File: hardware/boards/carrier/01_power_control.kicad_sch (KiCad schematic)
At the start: 34 parts, among them Q1 IPB020N10N5LF, Q2 2N7002, Q3 2N7002, U3 LMX5069MS, U4 INA237AIDGSR, U5 TCAN3413DR

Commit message: Update carrier for 1 oz fabrication
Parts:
- U3: footprint mini-rack-power:MSOP-10_3x3mm_P0.5mm_0.20mm_Clearance -> Package_SO:MSOP-10_3x3mm_P0.5mm
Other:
- note added: "U3 STOCK MSOP-10 FOOTPRINT U3 is Maxinmicro LMX5069MS (C47967145), MSOP-10; manufacturer datasheet is archived locally. Use Package_SO:MSOP-10_3x3mm_P0.5mm. Its 0.15 mm pad-to-pad gap is covered by a footprint-local board clearance override and is compatible with the selected 1 oz outer-copper fabrication process. Confirm vendor DFM before release."
- note removed: "PROJECT-LOCAL U3 FOOTPRINT U3 is Maxinmicro LMX5069MS (C47967145), MSOP-10; manufacturer datasheet is archived locally. Use mini-rack-power:MSOP-10_3x3mm_P0.5mm_0.20mm_Clearance. It retains KiCad's pad length, body, and courtyard, but narrows pads to 0.30 mm for 0.20 mm copper clearance at 0.50 mm pitch. This avoids the stock footprint's 0.15 mm clearance limit with 2 oz copper and satisfies the 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"
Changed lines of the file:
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@@
 		)
 	)
-	(text "PROJECT-LOCAL U3 FOOTPRINT\nU3 is Maxinmicro LMX5069MS (C47967145), MSOP-10; manufacturer datasheet is archived locally.\nUse mini-rack-power:MSOP-10_3x3mm_P0.5mm_0.20mm_Clearance. It retains KiCad's pad length, body, and courtyard,\nbut narrows pads to 0.30 mm for 0.20 mm copper clearance at 0.50 mm pitch. This avoids the stock footprint's 0.15 mm\nclearance limit with 2 oz copper and satisfies the project DRC rule. Confirm final copper weight and vendor DFM before release."
+	(text "U3 STOCK MSOP-10 FOOTPRINT\nU3 is Maxinmicro LMX5069MS (C47967145), MSOP-10; manufacturer datasheet is archived locally.\nUse Package_SO:MSOP-10_3x3mm_P0.5mm. Its 0.15 mm pad-to-pad gap is covered by a footprint-local board clearance\noverride and is compatible with the selected 1 oz outer-copper fabrication process. Confirm vendor DFM before release."
 		(exclude_from_sim no)
 		(at 93.98 76.2 0)
@@
 			)
 		)
-		(property "Footprint" "mini-rack-power:MSOP-10_3x3mm_P0.5mm_0.20mm_Clearance"
+		(property "Footprint" "Package_SO:MSOP-10_3x3mm_P0.5mm"
 			(at 148.59 28.956 0)
 			(hide yes)

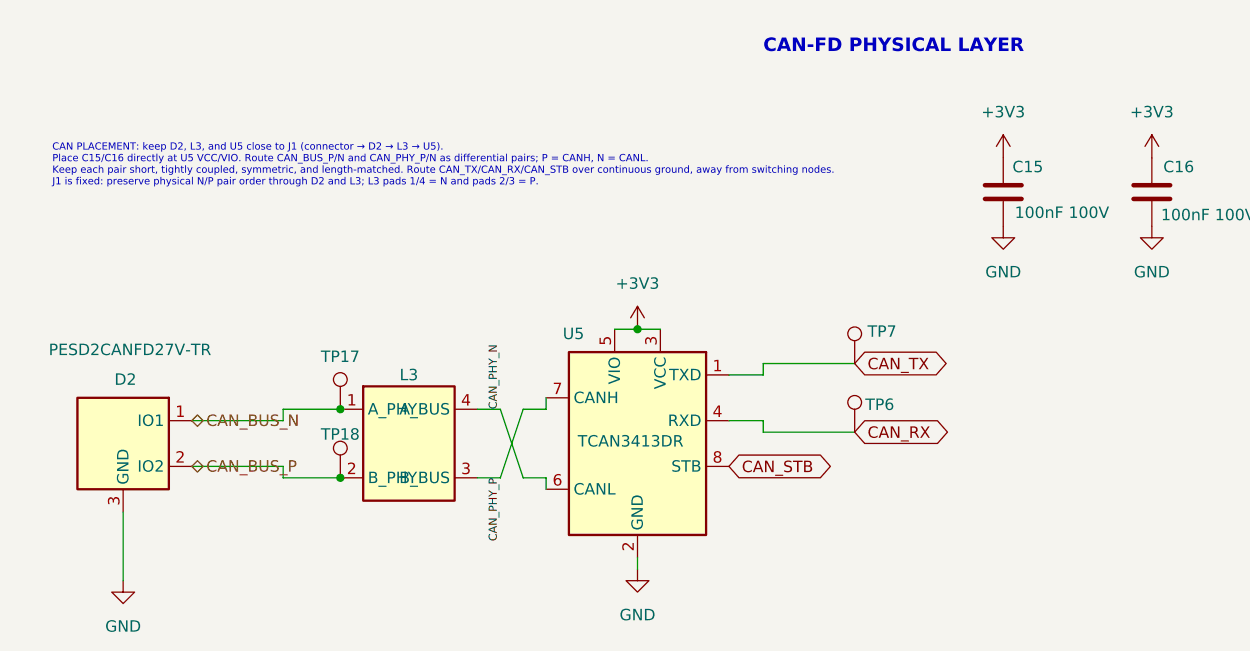
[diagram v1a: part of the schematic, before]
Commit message: Tie carrier CAN transceiver to normal mode
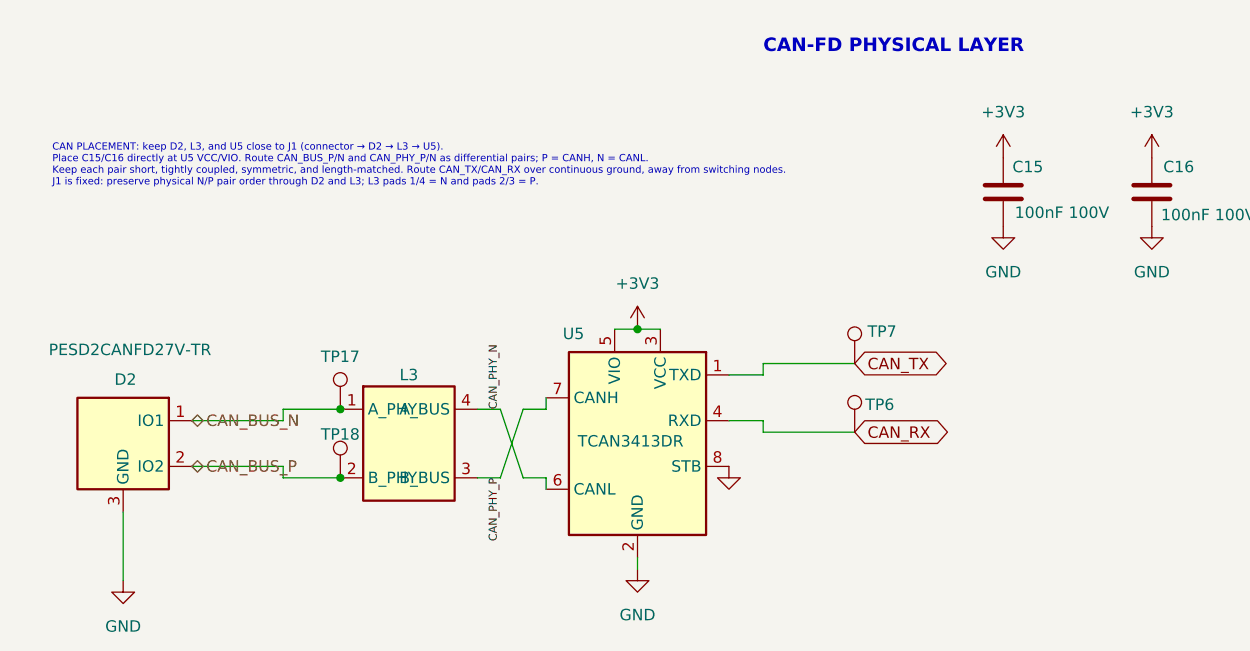
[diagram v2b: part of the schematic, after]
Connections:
- net CAN_STB is gone; now on net GND: U5.8 (STB)
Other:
- note added: "CAN PLACEMENT: keep D2, L3, and U5 close to J1 (connector → D2 → L3 → U5). Place C15/C16 directly at U5 VCC/VIO. Route CAN_BUS_P/N and CAN_PHY_P/N as differential pairs; P = CANH, N = CANL. Keep each pair short, tightly coupled, symmetric, and length-matched. Route CAN_TX/CAN_RX over continuous ground, away from switching nodes. J1 is fixed: preserve physical N/P pair order through D2 and L3; L3 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"
- note removed: "CAN PLACEMENT: keep D2, L3, and U5 close to J1 (connector → D2 → L3 → U5). Place C15/C16 directly at U5 VCC/VIO. Route CAN_BUS_P/N and CAN_PHY_P/N as differential pairs; P = CANH, N = CANL. Keep each pair short, tightly coupled, symmetric, and length-matched. Route CAN_TX/CAN_RX/CAN_STB over continuous ground, away from switching nodes. J1 is fixed: preserve physical N/P pair order through D2 and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"
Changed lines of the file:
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@@
 		)
 	)
-	(text "CAN PLACEMENT: keep D2, L3, and U5 close to J1 (connector → D2 → L3 → U5).\nPlace C15/C16 directly at U5 VCC/VIO. Route CAN_BUS_P/N and CAN_PHY_P/N as differential pairs; P = CANH, N = CANL.\nKeep each pair short, tightly coupled, symmetric, and length-matched. Route CAN_TX/CAN_RX/CAN_STB over continuous ground, away from switching nodes.\nJ1 is fixed: preserve physical N/P pair order through D2 and L3; L3 pads 1/4 = N and pads 2/3 = P."
+	(text "CAN PLACEMENT: keep D2, L3, and U5 close to J1 (connector → D2 → L3 → U5).\nPlace C15/C16 directly at U5 VCC/VIO. Route CAN_BUS_P/N and CAN_PHY_P/N as differential pairs; P = CANH, N = CANL.\nKeep each pair short, tightly coupled, symmetric, and length-matched. Route CAN_TX/CAN_RX over continuous ground, away from switching nodes.\nJ1 is fixed: preserve physical N/P pair order through D2 and L3; L3 pads 1/4 = N and pads 2/3 = P."
 		(exclude_from_sim no)
 		(at 23.876 221.742 0)
@@
 			)
 			(justify left bottom)
-		)
-	)
-	(global_label "CAN_STB"
-		(shape bidirectional)
-		(at 99.06 252.73 0)
-		(effects
-			(font
-				(size 1.27 1.27)
-			)
-			(justify left)
-		)
-		(property "Intersheetrefs" "${INTERSHEET_REFS}"
-			(at 99.06 252.73 0)
-			(hide yes)
-			(show_name no)
-			(do_not_autoplace no)
-			(effects
-				(font
-					(size 1.27 1.27)
-				)
-			)
 		)
 	)
@@
 					(unit 1)
 				)
+			)
+		)
+	)
+	(symbol
+		(lib_id "power:GND")
+		(at 99.06 252.73 0)
+		(unit 1)
+		(body_style 1)
+		(exclude_from_sim no)
+		(in_bom yes)
+		(on_board yes)
+		(in_pos_files yes)
+		(dnp no)
+		(fields_autoplaced yes)
+		(property "Reference" "#PWR0416"
+			(at 99.06 259.08 0)
+			(hide yes)
+			(show_name no)
+			(do_not_autoplace no)
+			(effects
+				(font
+					(size 1.27 1.27)
+				)
+			)
+		)
+		(property "Value" "GND"
+			(at 99.06 257.81 0)
+			(hide yes)
+			(show_name no)
+			(do_not_autoplace no)
+			(effects
+				(font
+					(size 1.27 1.27)
+				)
+			)
+		)
+		(property "Footprint" ""
+			(at 99.06 252.73 0)
+			(hide yes)
+			(show_name no)
+			(do_not_autoplace no)
+			(effects
+				(font
+					(size 1.27 1.27)
+				)
+			)
+		)
+		(property "Datasheet" ""
+			(at 99.06 252.73 0)
+			(hide yes)
+			(show_name no)
+			(do_not_autoplace no)
+			(effects
+				(font
+					(size 1.27 1.27)
+				)
+			)
+		)
+		(property "Description" "Power symbol creates a global label with name \"GND\" , ground"
+			(at 99.06 252.73 0)
+			(hide yes)
+			(show_name no)
+			(do_not_autoplace no)
+			(effects
+				(font
+					(size 1.27 1.27)
+				)
+			)
+		)
+		(pin "1"
+		)
+		(instances
+			(project "carrier"
+				(path "/ee42a069-09cc-4091-bee3-2dd6ab96c98c/bfe0cac3-96d7-4839-869d-6366daca24b5"
+					(reference "#PWR0416")
+					(unit 1)
+				)

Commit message: swap carrier CAN TVS signal pins
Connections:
- net CAN_BUS_N: now also D2.2 (IO2); no longer D2.1 (IO1)
- net CAN_BUS_P: now also D2.1 (IO1); no longer D2.2 (IO2)

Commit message: checkpoint: ALMOST DONE ROUTING
and then we get to find the DRC errors and fix silk ...
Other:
- moved on the sheet: D2
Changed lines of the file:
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@@
 	(wire
 		(pts
-			(xy 31.75 265.43) (xy 31.75 257.81)
+			(xy 29.21 265.43) (xy 29.21 257.81)
 		)
 		(stroke
@@
 	(wire
 		(pts
-			(xy 39.37 252.73) (xy 49.53 252.73)
+			(xy 176.53 53.34) (xy 160.02 53.34)
 		)
 		(stroke
@@
 	(wire
 		(pts
-			(xy 176.53 53.34) (xy 160.02 53.34)
+			(xy 76.2 254) (xy 78.74 254)
 		)
 		(stroke
@@
 	(wire
 		(pts
-			(xy 76.2 254) (xy 78.74 254)
+			(xy 388.62 38.1) (xy 388.62 40.64)
 		)
 		(stroke
@@
 	(wire
 		(pts
-			(xy 388.62 38.1) (xy 388.62 40.64)
+			(xy 36.83 247.65) (xy 49.53 247.65)
 		)
 		(stroke
@@
 	(wire
 		(pts
-			(xy 248.92 121.92) (xy 250.19 121.92)
+			(xy 36.83 252.73) (xy 49.53 252.73)
 		)
 		(stroke
@@
 	(wire
 		(pts
-			(xy 102.87 247.65) (xy 99.06 247.65)
+			(xy 248.92 121.92) (xy 250.19 121.92)
 		)
 		(stroke
@@
 	(wire
 		(pts
-			(xy 39.37 247.65) (xy 49.53 247.65)
+			(xy 102.87 247.65) (xy 99.06 247.65)
 		)
 		(stroke
@@
 	(hierarchical_label "CAN_BUS_P"
 		(shape bidirectional)
-		(at 39.37 252.73 0)
+		(at 36.83 252.73 0)
 		(effects
 			(font
@@
 	(hierarchical_label "CAN_BUS_N"
 		(shape bidirectional)
-		(at 39.37 247.65 0)
+		(at 36.83 247.65 0)
 		(effects
 			(font
@@
 	)
 	(symbol
-		(lib_id "power:GND")
-		(at 99.06 252.73 0)
-		(unit 1)
-		(body_style 1)
-		(exclude_from_sim no)
-		(in_bom yes)
-		(on_board yes)
-		(in_pos_files yes)
-		(dnp no)
-		(fields_autoplaced yes)
-		(property "Reference" "#PWR0416"
-			(at 99.06 259.08 0)
-			(hide yes)
-			(show_name no)
-			(do_not_autoplace no)
-			(effects
-				(font
-					(size 1.27 1.27)
-				)
-			)
-		)
-		(property "Value" "GND"
-			(at 99.06 257.81 0)
-			(hide yes)
-			(show_name no)
-			(do_not_autoplace no)
-			(effects
-				(font
-					(size 1.27 1.27)
-				)
-			)
-		)
-		(property "Footprint" ""
-			(at 99.06 252.73 0)
-			(hide yes)
-			(show_name no)
-			(do_not_autoplace no)
-			(effects
-				(font
-					(size 1.27 1.27)
-				)
-			)
-		)
-		(property "Datasheet" ""
-			(at 99.06 252.73 0)
-			(hide yes)
-			(show_name no)
-			(do_not_autoplace no)
-			(effects
-				(font
-					(size 1.27 1.27)
-				)
-			)
-		)
-		(property "Description" "Power symbol creates a global label with name \"GND\" , ground"
-			(at 99.06 252.73 0)
-			(hide yes)
-			(show_name no)
-			(do_not_autoplace no)
-			(effects
-				(font
-					(size 1.27 1.27)
-				)
-			)
-		)
-		(pin "1"
-		)
-		(instances
-			(project "carrier"
-				(path "/ee42a069-09cc-4091-bee3-2dd6ab96c98c/bfe0cac3-96d7-4839-869d-6366daca24b5"
-					(reference "#PWR0416")
-					(unit 1)
-				)
-			)
-		)
-	)
-	(symbol
 		(lib_id "backplane-backpack:TCAN3413DR")
 		(at 88.9 250.19 0)
@@
 	(symbol
 		(lib_id "power:GND")
-		(at 31.75 265.43 0)
+		(at 29.21 265.43 0)
 		(unit 1)
 		(body_style 1)
@@
 		(fields_autoplaced yes)
 		(property "Reference" "#PWR0411"
-			(at 31.75 271.78 0)
+			(at 29.21 271.78 0)
 			(hide yes)
 			(show_name no)
@@
 		)
 		(property "Value" "GND"
-			(at 31.75 270.51 0)
+			(at 29.21 270.51 0)
 			(show_name no)
 			(do_not_autoplace no)
@@
 		)
 		(property "Footprint" ""
-			(at 31.75 265.43 0)
+			(at 29.21 265.43 0)
 			(hide yes)
 			(show_name no)
@@
 		)
 		(property "Datasheet" ""
-			(at 31.75 265.43 0)
+			(at 29.21 265.43 0)
 			(hide yes)
 			(show_name no)
@@
 		)
 		(property "Description" "Power symbol creates a global label with name \"GND\" , ground"
-			(at 31.75 265.43 0)
+			(at 29.21 265.43 0)
 			(hide yes)
 			(show_name no)
@@
 	(symbol
 		(lib_id "backplane-backpack:PESD_Dual_SOT23")
-		(at 31.75 250.19 0)
+		(at 29.21 250.19 0)
 		(mirror y)
 		(unit 1)
@@
 		(dnp no)
 		(property "Reference" "D2"
-			(at 32.004 243.078 0)
+			(at 29.464 243.078 0)
 			(show_name no)
 			(do_not_autoplace no)
@@
 		)
 		(property "Value" "PESD2CANFD27V-TR"
-			(at 32.512 239.776 0)
+			(at 29.972 239.776 0)
 			(show_name no)
 			(do_not_autoplace no)
@@
 		)
 		(property "Footprint" "Package_TO_SOT_SMD:SOT-23"
-			(at 31.75 245.11 0)
+			(at 29.21 245.11 0)
 			(hide yes)
 			(show_name no)
@@
 		)
 		(property "Datasheet" "https://assets.nexperia.com/documents/data-sheet/PESD2CANFD27V-T.pdf"
-			(at 31.75 242.57 0)
+			(at 29.21 242.57 0)
 			(hide yes)
 			(show_name no)
@@
 		)
 		(property "Description" "Dual-line shunt TVS/ESD protector, signal pins 1/2 and common ground pin 3"
-			(at 31.75 240.03 0)
+			(at 29.21 240.03 0)
 			(hide yes)
 			(show_name no)
@@
 		)
 		(property "MPN" "PESD2CANFD27V-TR"
-			(at 31.75 250.19 0)
+			(at 29.21 250.19 0)
 			(hide yes)
 			(show_name no)
@@
 		)
 		(property "LCSC" "C552488"
-			(at 31.75 250.19 0)
+			(at 29.21 250.19 0)
 			(hide yes)
 			(show_name no)
@@
 		)
 		(property "Package" "SOT-23"
-			(at 31.75 250.19 0)
+			(at 29.21 250.19 0)
 			(hide yes)
 			(show_name no)
@@
 		)
 		(property "Population" "POP"
-			(at 31.75 250.19 0)
+			(at 29.21 250.19 0)
 			(hide yes)
 			(show_name no)
@@
 		)
 		(property "Manufacturer" "Nexperia"
-			(at 31.75 250.19 0)
+			(at 29.21 250.19 0)
 			(hide yes)
 			(show_name no)
@@
 					(unit 1)
 				)
+			)
+		)
+	)
+	(symbol
+		(lib_id "power:GND")
+		(at 99.06 252.73 0)
+		(unit 1)
+		(body_style 1)
+		(exclude_from_sim no)
+		(in_bom yes)
+		(on_board yes)
+		(in_pos_files yes)
+		(dnp no)
+		(fields_autoplaced yes)
+		(property "Reference" "#PWR0416"
+			(at 99.06 259.08 0)
+			(hide yes)
+			(show_name no)
+			(do_not_autoplace no)
+			(effects
+				(font
+					(size 1.27 1.27)
+				)
+			)
+		)
+		(property "Value" "GND"
+			(at 99.06 257.81 0)
+			(hide yes)
+			(show_name no)
+			(do_not_autoplace no)
+			(effects
+				(font
+					(size 1.27 1.27)
+				)
+			)
+		)
+		(property "Footprint" ""
+			(at 99.06 252.73 0)
+			(hide yes)
+			(show_name no)
+			(do_not_autoplace no)
+			(effects
+				(font
+					(size 1.27 1.27)
+				)
+			)
+		)
+		(property "Datasheet" ""
+			(at 99.06 252.73 0)
+			(hide yes)
+			(show_name no)
+			(do_not_autoplace no)
+			(effects
+				(font
+					(size 1.27 1.27)
+				)
+			)
+		)
+		(property "Description" "Power symbol creates a global label with name \"GND\" , ground"
+			(at 99.06 252.73 0)
+			(hide yes)
+			(show_name no)
+			(do_not_autoplace no)
+			(effects
+				(font
+					(size 1.27 1.27)
+				)
+			)
+		)
+		(pin "1"
+		)
+		(instances
+			(project "carrier"
+				(path "/ee42a069-09cc-4091-bee3-2dd6ab96c98c/bfe0cac3-96d7-4839-869d-6366daca24b5"
+					(reference "#PWR0416")
+					(unit 1)
+				)

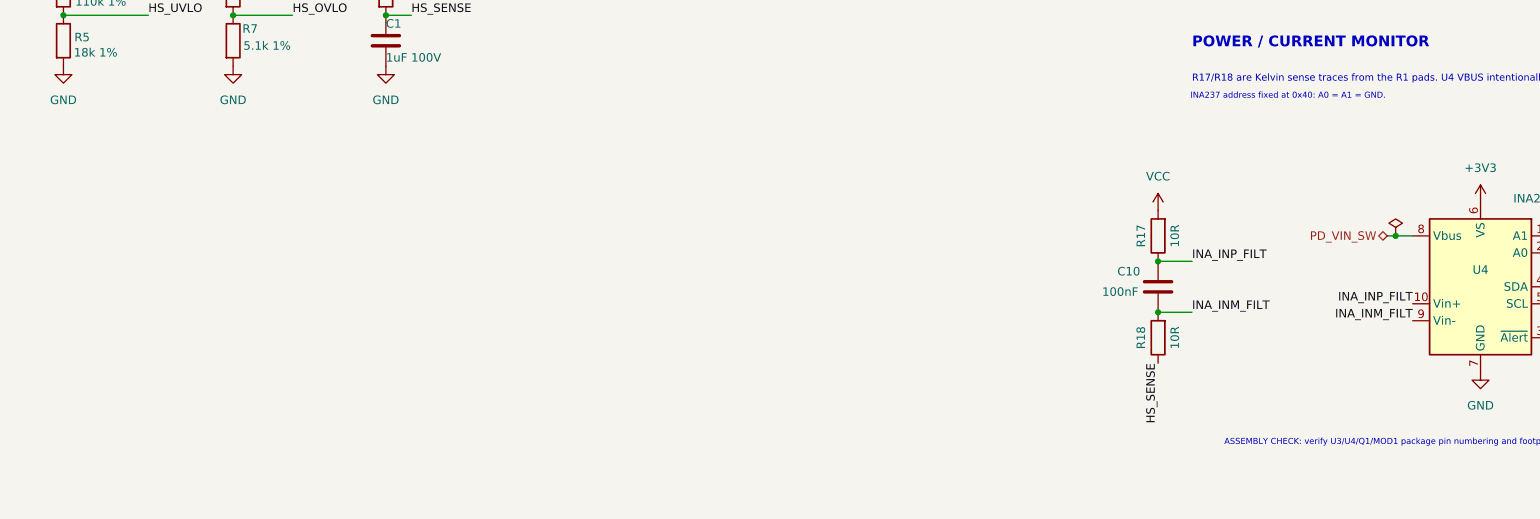
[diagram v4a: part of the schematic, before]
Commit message: add carrier bring-up testpoints
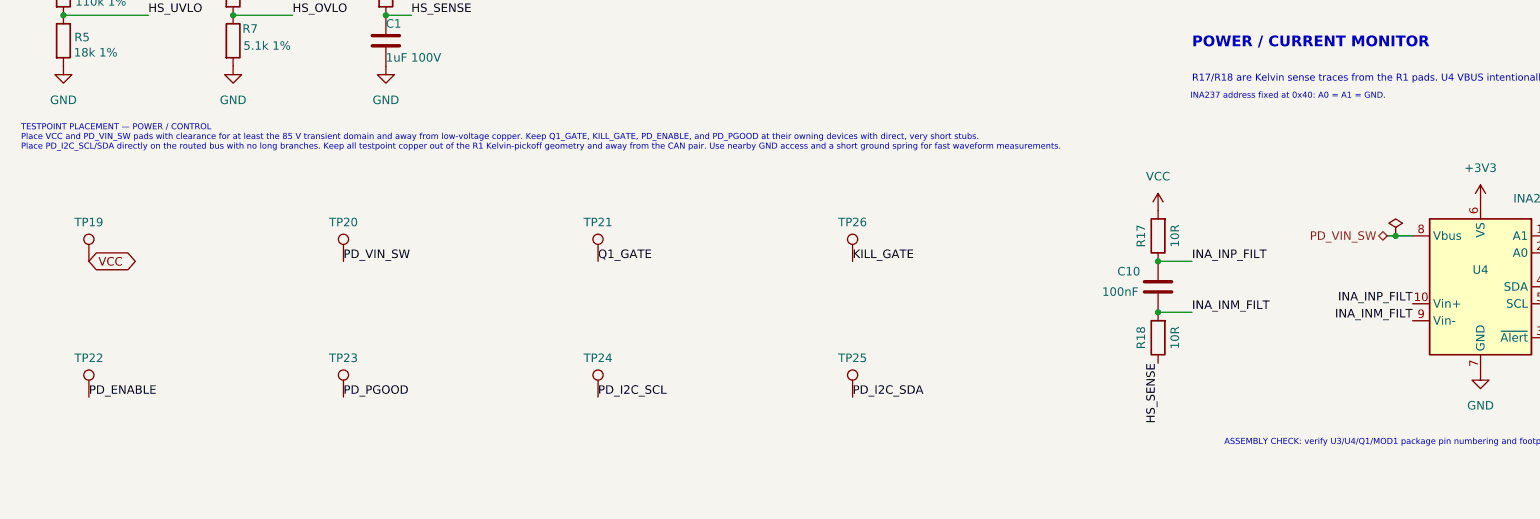
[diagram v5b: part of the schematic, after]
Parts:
- added TP19: VCC, TestPoint:TestPoint_Pad_D1.5mm, symbol Connector:TestPoint
- added TP20: PD_VIN_SW, TestPoint:TestPoint_Pad_D1.5mm, symbol Connector:TestPoint
- added TP21: Q1_GATE, TestPoint:TestPoint_Pad_D1.5mm, symbol Connector:TestPoint
- added TP22: PD_ENABLE, TestPoint:TestPoint_Pad_D1.5mm, symbol Connector:TestPoint
- added TP23: PD_PGOOD, TestPoint:TestPoint_Pad_D1.5mm, symbol Connector:TestPoint
- added TP24: PD_I2C_SCL, TestPoint:TestPoint_Pad_D1.5mm, symbol Connector:TestPoint
- added TP25: PD_I2C_SDA, TestPoint:TestPoint_Pad_D1.5mm, symbol Connector:TestPoint
- added TP26: KILL_GATE, TestPoint:TestPoint_Pad_D1.5mm, symbol Connector:TestPoint
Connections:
- net KILL_GATE: now also TP26.1
- net PD_ENABLE: now also TP22.1
- net PD_I2C_SCL: now also TP24.1
- net PD_I2C_SDA: now also TP25.1
- net PD_PGOOD: now also TP23.1
- net PD_VIN_SW: now also TP20.1
- net Q1_GATE: now also TP21.1
- net VCC: now also TP19.1
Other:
- note added: "TESTPOINT PLACEMENT — POWER / CONTROL Place VCC and PD_VIN_SW pads with clearance for at least the 85 V transient domain and away from low-voltage copper. Keep Q1_GATE, KILL_GATE, PD_ENABLE, and PD_PGOOD at their owning devices with direct, very short stubs. Place PD_I2C_SCL/SDA directly on the routed bus with no long branches. Keep all testpoint copper out of the R1 Kelvin-pickoff geometry and a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"

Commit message: scope carrier D2 pin mapping symbol
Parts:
- D2: symbol backplane-backpack:PESD_Dual_SOT23 -> backplane-backpack:PESD_Dual_SOT23_IO1_Bottom
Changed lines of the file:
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@@
 	)
 	(symbol
-		(lib_id "backplane-backpack:PESD_Dual_SOT23")
+		(lib_id "backplane-backpack:PESD_Dual_SOT23_IO1_Bottom")
 		(at 29.21 250.19 0)
 		(mirror y)
